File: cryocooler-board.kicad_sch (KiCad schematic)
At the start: 50 parts, among them J1 MOL Pico 4, J2 MOL Pico 4, J3 MOL Pico 4, J4 MOL Pico 4, Q1 IPZ40N04S5-3R1, Q2 IPZ40N04S5-3R1, U1 PTPS55288RPMR, U2 AD5258BRMZ1, U3 C1T 4

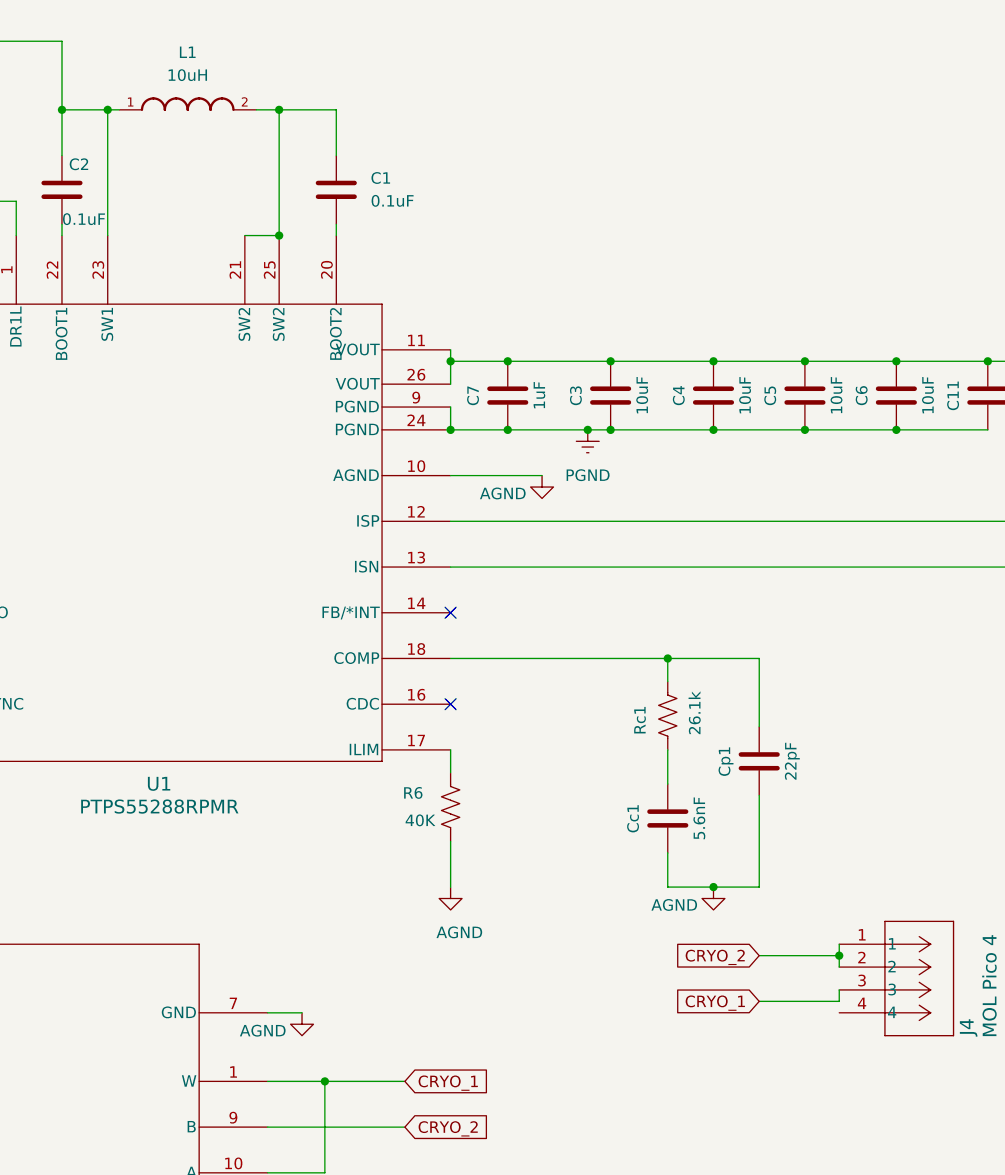
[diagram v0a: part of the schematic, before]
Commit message: Reorganize libraries: lib/Cryocooler symbols, footprints and 3D models; custom NT1 net tie; L1 symbol corrected to XAL1010-103MED; add 2-pin Molex for future use
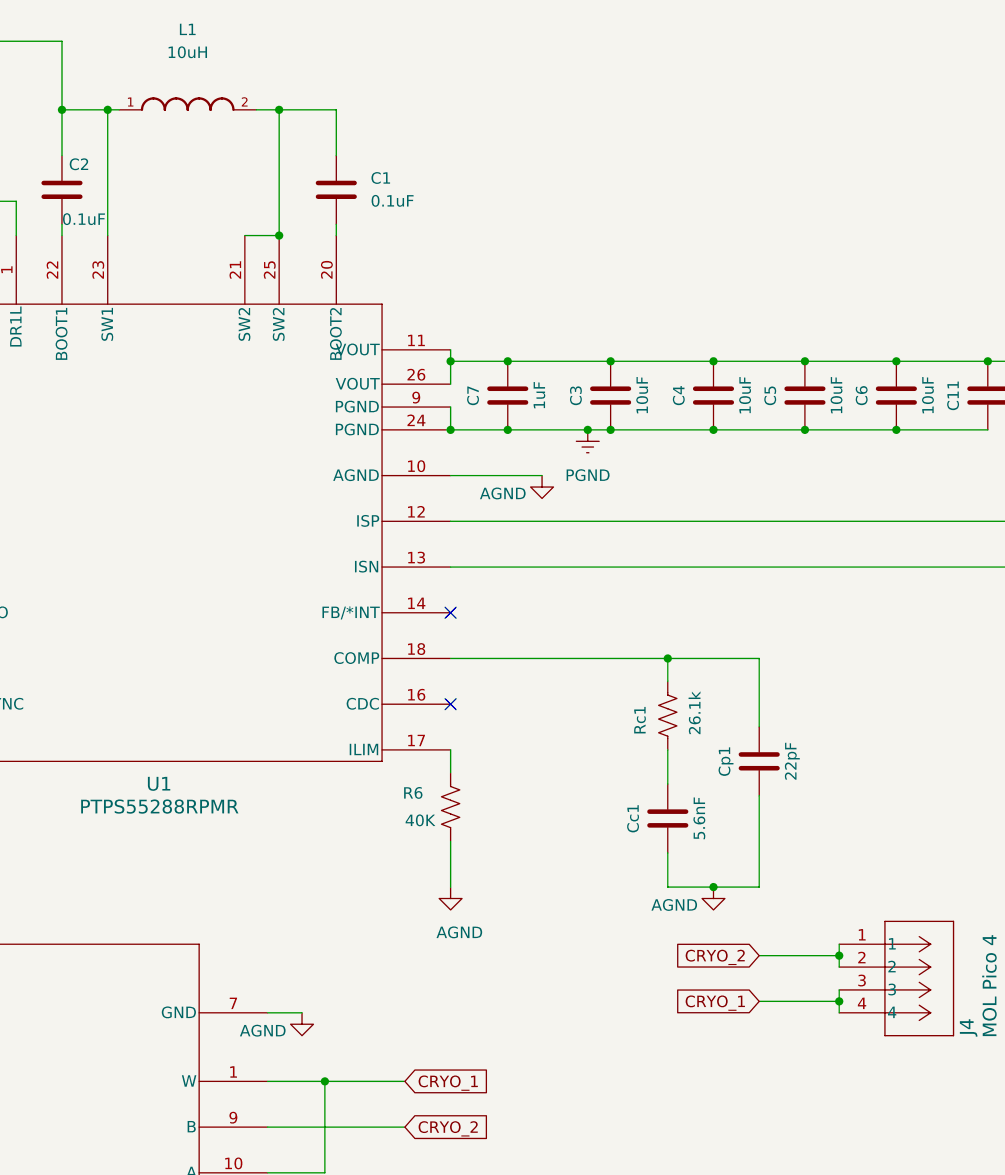
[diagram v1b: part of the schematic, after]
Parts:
- C1, C10, C2, C9: footprint Cryocooler_footprints:GCM21BR72A104KA37L -> Cryocooler:GCM21BR72A104KA37L
- C11, CIN3: footprint Cryocooler_footprints:EEH-ZA1V680XP -> Cryocooler:EEH-ZA1V680XP
- C3, C4, C5, C6, CIN1, CIN2: footprint Cryocooler_footprints:CGA5L1X7R1H106K160AC -> Cryocooler:CGA5L1X7R1H106K160AC
- C7, C8, CIN4: footprint Cryocooler_footprints:CGA3E3X5R1H105M080AB -> Cryocooler:CGA3E3X5R1H105M080AB
- CVCC1: footprint Cryocooler_footprints:GRT188R61C475KE13D -> Cryocooler:GRT188R61C475KE13D
- Cc1: footprint Cryocooler_footprints:CGA3E2C0G1H562J080AA -> Cryocooler:CGA3E2C0G1H562J080AA
- Cdith1: footprint Cryocooler_footprints:CGA3E2X7R1H473K080AD -> Cryocooler:CGA3E2X7R1H473K080AD
- Cp1: footprint Cryocooler_footprints:CGA3E2NP01H220J080AA -> Cryocooler:CGA3E2NP01H220J080AA
- H1, H2, H3, H4: footprint Cryocooler_footprints:M3_3_4mm_hole -> Cryocooler:M3_3_4mm_hole
- J1, J2, J3, J4: footprint Cryocooler_footprints:MOLEX_4_pin -> Cryocooler:MOLEX_4_pin; symbol MOLEX_4_pin:5040500491 -> Cryocooler:5040500491
- L1: footprint Cryocooler_footprints:XAL1010 -> Cryocooler:XAL1010; symbol XAL1010-472MED:XAL1010-472MED -> Cryocooler:XAL1010-103MED; AVAILABILITY In Stock -> (none); Availability In Stock -> (none); Check_prices https://www.coilcraft.com/en-us/products/power/shielded-ind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 -> (none); DESCRIPTION 10 µH Shielded Molded Inductor 17.5 A 5.7mOhm Max Nonstanda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 -> (none); Description_1 10 µH Shielded Molded Inductor 17.5 A 5.7mOhm Max Nonstanda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 -> (none); LCSC Part # (none) -> C6358489; MP XAL1010-103MED -> (none); PACKAGE None -> (none); PRICE None -> (none); PURCHASE-URL https://www.coilcraft.com/en-us/products/power/shielded-ind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 -> (none); Package None -> (none); Price None -> (none); SnapEDA_Link https://www.snapeda.com/parts/XAL1010-472MED/Coilcraft/view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 -> (none)
- NT1: footprint NetTie:NetTie-2_SMD_Pad0.5mm -> Cryocooler:NetTie-2_SMD_Pad0.3mm
- Q1, Q2: footprint Cryocooler_footprints:IPZ40N04S5L4R8ATMA1 -> Cryocooler:IPZ40N04S5L4R8ATMA1; symbol IPZ40N04S5-3R1:IPZ40N04S5-3R1 -> Cryocooler:IPZ40N04S5-3R1
- R1, R2: footprint Cryocooler_footprints:CRCW12062K20JNEA -> Cryocooler:CRCW12062K20JNEA
- R3: footprint Cryocooler_footprints:CRF1206-FZ-R010ELF -> Cryocooler:CRF1206-FZ-R010ELF
- R4: footprint Cryocooler_footprints:CRCW080530K9FKEA -> Cryocooler:CRCW080530K9FKEA
- R5: footprint Cryocooler_footprints:CRCW08052K00FKEA -> Cryocooler:CRCW08052K00FKEA
- R6: footprint Cryocooler_footprints:CRCW120620K0FKEAC -> Cryocooler:CRCW120620K0FKEAC
- R7, R8: footprint Cryocooler_footprints:CRCW08051R00JNEAHP -> Cryocooler:CRCW08051R00JNEAHP
- Rc1: footprint Cryocooler_footprints:CRCW060326K1FKEA -> Cryocooler:CRCW060326K1FKEA
- Rfsw1: footprint Cryocooler_footprints:CRCW060310K0FKEA -> Cryocooler:CRCW060310K0FKEA
- TP_AGND1, TP_PGND1, TP_SCL1, TP_SDA1, TP_VIN1, TP_VOUT1: now left out of the parts list
- U1: footprint Cryocooler_footprints:TPS55288 -> Cryocooler:TPS55288; symbol 2025-07-07_17-23-20:PTPS55288RPMR -> Cryocooler:PTPS55288RPMR
- U2: footprint Cryocooler_footprints:AD5258BRMZ1_IC -> Cryocooler:AD5258BRMZ1_IC; symbol AD5258BRMZ1:AD5258BRMZ1 -> Cryocooler:AD5258BRMZ1
- U3: footprint Cryocooler_footprints:0685T4000-01 -> Cryocooler:0685T4000-01; symbol 0685T4000-01:C1T_4 -> Cryocooler:C1T_4
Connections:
- net CRYO_1: now also J4.4

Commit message: V4.1:Cryocooler VOUT connector changed to 2-pin Pico-Lock 2053380002 (J5); R3 and TP_VOUT1 moved
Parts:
- removed J2: MOL Pico 4, Cryocooler:MOLEX_4_pin, symbol Cryocooler:5040500491
- added J2: MOL Pico 2, Cryocooler:MOLEX_2_pin, symbol Cryocooler:2053380002
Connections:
- net PGND: now also J2.2
- net VOUT: now also J2.1
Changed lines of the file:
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@@
 	)
 	(junction
-		(at 44.45 153.67)
-		(diameter 0)
-		(color 0 0 0 0)
-	)
-	(junction
 		(at 92.71 92.71)
 		(diameter 0)
@@
 	)
 	(junction
-		(at 52.07 153.67)
-		(diameter 0)
-		(color 0 0 0 0)
-	)
-	(junction
 		(at 187.96 85.09)
 		(diameter 0)
@@
 	(wire
 		(pts
-			(xy 44.45 153.67) (xy 46.99 153.67)
-		)
-		(stroke
-			(width 0)
-			(type default)
-		)
-	)
-	(wire
-		(pts
 			(xy 52.07 80.01) (xy 62.23 80.01)
 		)
@@
 	(wire
 		(pts
+			(xy 49.53 144.78) (xy 52.07 144.78)
+		)
+		(stroke
+			(width 0)
+			(type default)
+		)
+	)
+	(wire
+		(pts
+			(xy 49.53 144.78) (xy 49.53 158.75)
+		)
+		(stroke
+			(width 0)
+			(type default)
+		)
+	)
+	(wire
+		(pts
 			(xy 264.16 77.47) (xy 264.16 100.33)
 		)
@@
 	(wire
 		(pts
-			(xy 44.45 144.78) (xy 44.45 153.67)
-		)
-		(stroke
-			(width 0)
-			(type default)
-		)
-	)
-	(wire
-		(pts
 			(xy 231.14 142.24) (xy 231.14 143.51)
 		)
@@
 	(wire
 		(pts
-			(xy 46.99 158.75) (xy 46.99 153.67)
+			(xy 46.99 144.78) (xy 46.99 158.75)
 		)
 		(stroke
@@
 	(wire
 		(pts
-			(xy 49.53 153.67) (xy 52.07 153.67)
-		)
-		(stroke
-			(width 0)
-			(type default)
-		)
-	)
-	(wire
-		(pts
 			(xy 231.14 148.59) (xy 231.14 147.32)
 		)
@@
 	(wire
 		(pts
-			(xy 44.45 158.75) (xy 44.45 153.67)
-		)
-		(stroke
-			(width 0)
-			(type default)
-		)
-	)
-	(wire
-		(pts
 			(xy 85.09 147.32) (xy 95.25 147.32)
 		)
@@
 	(wire
 		(pts
-			(xy 52.07 149.86) (xy 52.07 153.67)
-		)
-		(stroke
-			(width 0)
-			(type default)
-		)
-	)
-	(wire
-		(pts
 			(xy 194.31 85.09) (xy 203.2 85.09)
 		)
@@
 	(wire
 		(pts
-			(xy 52.07 153.67) (xy 52.07 158.75)
-		)
-		(stroke
-			(width 0)
-			(type default)
-		)
-	)
-	(wire
-		(pts
 			(xy 231.14 143.51) (xy 231.14 144.78)
 		)
@@
 	(wire
 		(pts
-			(xy 49.53 153.67) (xy 49.53 158.75)
-		)
-		(stroke
-			(width 0)
-			(type default)
-		)
-	)
-	(wire
-		(pts
 			(xy 205.74 85.09) (xy 217.17 85.09)
 		)
@@
 	(wire
 		(pts
+			(xy 43.18 144.78) (xy 46.99 144.78)
+		)
+		(stroke
+			(width 0)
+			(type default)
+		)
+	)
+	(wire
+		(pts
 			(xy 255.27 77.47) (xy 255.27 95.25)
 		)
@@
 	(wire
 		(pts
-			(xy 46.99 144.78) (xy 44.45 144.78)
-		)
-		(stroke
-			(width 0)
-			(type default)
-		)
-	)
-	(wire
-		(pts
 			(xy 22.86 76.2) (xy 22.86 80.01)
 		)
@@
 		)
 	)
-	(label "Viout_GND"
-		(at 44.45 153.67 90)
+	(label "Vout_GND"
+		(at 43.18 144.78 90)
 		(fields_autoplaced yes)
 		(effects
@@
 	(global_label "VOUT"
 		(shape input)
-		(at 52.07 149.86 90)
+		(at 52.07 144.78 90)
 		(fields_autoplaced yes)
 		(effects
@@
 		)
 		(property "Intersheetrefs" "${INTERSHEET_REFS}"
-			(at 52.07 142.1576 90)
+			(at 52.07 137.0776 90)
 			(effects
 				(font
@@
 	(symbol
 		(lib_id "power:Earth")
-		(at 46.99 144.78 0)
+		(at 43.18 144.78 0)
 		(unit 1)
 		(exclude_from_sim no)
@@
 		(fields_autoplaced yes)
 		(property "Reference" "#PWR07"
-			(at 46.99 151.13 0)
+			(at 43.18 151.13 0)
 			(effects
 				(font
@@
 		)
 		(property "Value" "PGND"
-			(at 46.99 149.86 0)
+			(at 43.18 149.86 0)
 			(effects
 				(font
@@
 		)
 		(property "Footprint" ""
-			(at 46.99 144.78 0)
+			(at 43.18 144.78 0)
 			(effects
 				(font
@@
 		)
 		(property "Datasheet" "~"
-			(at 46.99 144.78 0)
+			(at 43.18 144.78 0)
 			(effects
 				(font
@@
 		)
 		(property "Description" "Power symbol creates a global label with name \"Earth\""
-			(at 46.99 144.78 0)
+			(at 43.18 144.78 0)
 			(effects
 				(font
@@
 	)
 	(symbol
+		(lib_id "Cryocooler:2053380002")
+		(at 49.53 158.75 270)
+		(unit 1)
+		(exclude_from_sim no)
+		(in_bom yes)
+		(on_board yes)
+		(dnp no)
+		(property "Reference" "J2"
+			(at 42.418 173.736 90)
+			(effects
+				(font
+					(size 1.524 1.524)
+				)
+				(justify left)
+			)
+		)
+		(property "Value" "MOL Pico 2"
+			(at 42.418 176.276 90)
+			(effects
+				(font
+					(size 1.524 1.524)
+				)
+				(justify left)
+			)
+		)
+		(property "Footprint" "Cryocooler:MOLEX_2_pin"
+			(at 49.53 158.75 0)
+			(effects
+				(font
+					(size 1.27 1.27)
+					(italic yes)
+				)
+				(hide yes)
+			)
+		)
+		(property "Datasheet" "https://www.molex.com/en-us/products/part-detail-pdf/2053380002?display=pdf"
+			(at 49.53 158.75 0)
+			(effects
+				(font
+					(size 1.27 1.27)
+					(italic yes)
+				)
+				(hide yes)
+			)
+		)
+		(property "Description" ""
+			(at 49.53 158.75 0)
+			(effects
+				(font
+					(size 1.27 1.27)
+				)
+				(hide yes)
+			)
+		)
+		(pin "2"
+		)
+		(pin "1"
+		)
+		(instances
+			(project ""
+				(path "/fc4eef0c-f0fe-4c26-9eed-35cfade9960a"
+					(reference "J2")
+					(unit 1)
+				)
+			)
+		)
+	)
+	(symbol
 		(lib_id "power:Earth")
 		(at 203.2 85.09 0)
@@
 					(unit 1)
 				)
-			)
-		)
-	)
-	(symbol
-		(lib_id "Cryocooler:5040500491")
-		(at 52.07 158.75 270)
-		(unit 1)
-		(exclude_from_sim no)
-		(in_bom yes)
-		(on_board yes)
-		(dnp no)
-		(property "Reference" "J2"
-			(at 41.91 172.974 90)
-			(effects
-				(font
-					(size 1.524 1.524)
-				)
-				(justify left)
-			)
-		)
-		(property "Value" "MOL Pico 4"
-			(at 41.656 175.768 90)
-			(effects
-				(font
-					(size 1.524 1.524)
-				)
-				(justify left)
-			)
-		)
-		(property "Footprint" "Cryocooler:MOLEX_4_pin"
-			(at 52.07 158.75 0)
-			(effects
-				(font
-					(size 1.27 1.27)
-					(italic yes)
-				)
-				(hide yes)
-			)
-		)
-		(property "Datasheet" "https://www.molex.com/en-us/products/part-detail-pdf/5040500491?display=pdf"
-			(at 52.07 158.75 0)
-			(effects
-				(font
-					(size 1.27 1.27)
-					(italic yes)
-				)
-				(hide yes)
-			)
-		)
-		(property "Description" ""
-			(at 52.07 158.75 0)
-			(effects
-				(font
-					(size 1.27 1.27)
-				)
-				(hide yes)
-			)
-		)
-		(pin "3"
-		)
-		(pin "2"
-		)
-		(pin "1"
-		)
-		(pin "4"
-		)
-		(instances
-			(project "try_1_tps5288"
-				(path "/fc4eef0c-f0fe-4c26-9eed-35cfade9960a"
-					(reference "J2")
-					(unit 1)
-				)

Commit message: V4.1: J4 (cryocooler set point) back to 2-pin Pico-Lock 2053380002; CRYO_1/CRYO_2 rerouted
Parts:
- J4: value MOL Pico 4 -> MOL Pico 2; footprint Cryocooler:MOLEX_4_pin -> Cryocooler:MOLEX_2_pin; symbol Cryocooler:5040500491 -> Cryocooler:2053380002
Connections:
- net CRYO_1: now also J4.2; no longer J4.3, J4.4
- net CRYO_2: no longer J4.2
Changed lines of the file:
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@@
-	)
-	(junction
-		(at 231.14 143.51)
-		(diameter 0)
-		(color 0 0 0 0)
 	)
 	(junction
@@
 	(junction
 		(at 168.91 49.53)
-		(diameter 0)
-		(color 0 0 0 0)
-	)
-	(junction
-		(at 231.14 148.59)
 		(diameter 0)
 		(color 0 0 0 0)
@@
 	(wire
 		(pts
-			(xy 231.14 142.24) (xy 231.14 143.51)
-		)
-		(stroke
-			(width 0)
-			(type default)
-		)
-	)
-	(wire
-		(pts
 			(xy 73.66 92.71) (xy 73.66 95.25)
 		)
@@
 	(wire
 		(pts
-			(xy 231.14 148.59) (xy 231.14 147.32)
-		)
-		(stroke
-			(width 0)
-			(type default)
-		)
-	)
-	(wire
-		(pts
 			(xy 123.19 97.79) (xy 110.49 97.79)
 		)
@@
 	(wire
 		(pts
-			(xy 231.14 148.59) (xy 231.14 149.86)
-		)
-		(stroke
-			(width 0)
-			(type default)
-		)
-	)
-	(wire
-		(pts
 			(xy 100.33 152.4) (xy 100.33 147.32)
 		)
@@
 	(wire
 		(pts
+			(xy 222.25 148.59) (xy 222.25 147.32)
+		)
+		(stroke
+			(width 0)
+			(type default)
+		)
+	)
+	(wire
+		(pts
 			(xy 109.22 69.85) (xy 109.22 80.01)
 		)
@@
 	(wire
 		(pts
+			(xy 222.25 144.78) (xy 227.33 144.78)
+		)
+		(stroke
+			(width 0)
+			(type default)
+		)
+	)
+	(wire
+		(pts
 			(xy 194.31 85.09) (xy 203.2 85.09)
 		)
@@
 	(wire
 		(pts
-			(xy 222.25 148.59) (xy 231.14 148.59)
+			(xy 222.25 143.51) (xy 222.25 144.78)
 		)
 		(stroke
@@
 	(wire
 		(pts
-			(xy 231.14 143.51) (xy 231.14 144.78)
-		)
-		(stroke
-			(width 0)
-			(type default)
-		)
-	)
-	(wire
-		(pts
 			(xy 85.09 157.48) (xy 95.25 157.48)
 		)
@@
 	(wire
 		(pts
-			(xy 222.25 143.51) (xy 231.14 143.51)
-		)
-		(stroke
-			(width 0)
-			(type default)
-		)
-	)
-	(wire
-		(pts
 			(xy 71.12 153.67) (xy 71.12 158.75)
 		)
@@
 		(pts
 			(xy 109.22 41.91) (xy 144.78 41.91)
+		)
+		(stroke
+			(width 0)
+			(type default)
+		)
+	)
+	(wire
+		(pts
+			(xy 222.25 147.32) (xy 227.33 147.32)
 		)
 		(stroke
@@
 	)
 	(symbol
-		(lib_id "Cryocooler:5040500491")
-		(at 231.14 142.24 0)
+		(lib_id "Cryocooler:2053380002")
+		(at 227.33 144.78 0)
 		(unit 1)
 		(exclude_from_sim no)
@@
 		(dnp no)
 		(property "Reference" "J4"
-			(at 245.364 152.4 90)
+			(at 241.554 154.94 90)
 			(effects
 				(font
@@
 			)
 		)
-		(property "Value" "MOL Pico 4"
-			(at 247.904 152.654 90)
+		(property "Value" "MOL Pico 2"
+			(at 244.094 155.194 90)
 			(effects
 				(font
@@
 			)
 		)
-		(property "Footprint" "Cryocooler:MOLEX_4_pin"
-			(at 231.14 142.24 0)
+		(property "Footprint" "Cryocooler:MOLEX_2_pin"
+			(at 227.33 144.78 0)
 			(effects
 				(font
@@
 			)
 		)
-		(property "Datasheet" "https://www.molex.com/en-us/products/part-detail-pdf/5040500491?display=pdf"
-			(at 231.14 142.24 0)
+		(property "Datasheet" "https://www.molex.com/en-us/products/part-detail-pdf/2053380002?display=pdf"
+			(at 227.33 144.78 0)
 			(effects
 				(font
@@
 		)
 		(property "Description" ""
-			(at 231.14 142.24 0)
-			(effects
-				(font
-					(size 1.27 1.27)
-				)
-				(hide yes)
-			)
-		)
-		(pin "3"
+			(at 227.33 144.78 0)
+			(effects
+				(font
+					(size 1.27 1.27)
+				)
+				(hide yes)
+			)
 		)
 		(pin "2"
@@
 		(pin "1"
 		)
-		(pin "4"
-		)
 		(instances

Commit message: V4.1: R1/R2 (I2C pull-ups) DNP for 3.3 V host; exclude DNP parts from JLC output; J4 value fixed
README: I2C level issue added to open items (provisional decision)
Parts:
- R1, R2: now not fitted
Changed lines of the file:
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@@
 		(in_bom yes)
 		(on_board yes)
-		(dnp no)
+		(dnp yes)
 		(fields_autoplaced yes)
 		(property "Reference" "R1"
@@
 		(in_bom yes)
 		(on_board yes)
-		(dnp no)
+		(dnp yes)
 		(property "Reference" "R2"
 			(at 106.172 87.376 0)
